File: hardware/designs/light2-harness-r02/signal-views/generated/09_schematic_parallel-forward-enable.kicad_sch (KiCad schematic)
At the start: 45 parts, among them J2 ESP32-P4 Right Header (EXT1), J3 ESP32-P4 Left Header (EXT2), U1 SN74LVC244AN, U2 SN74LVC244AN, U3 SN74LV125AN, U4 SN74LV125AN

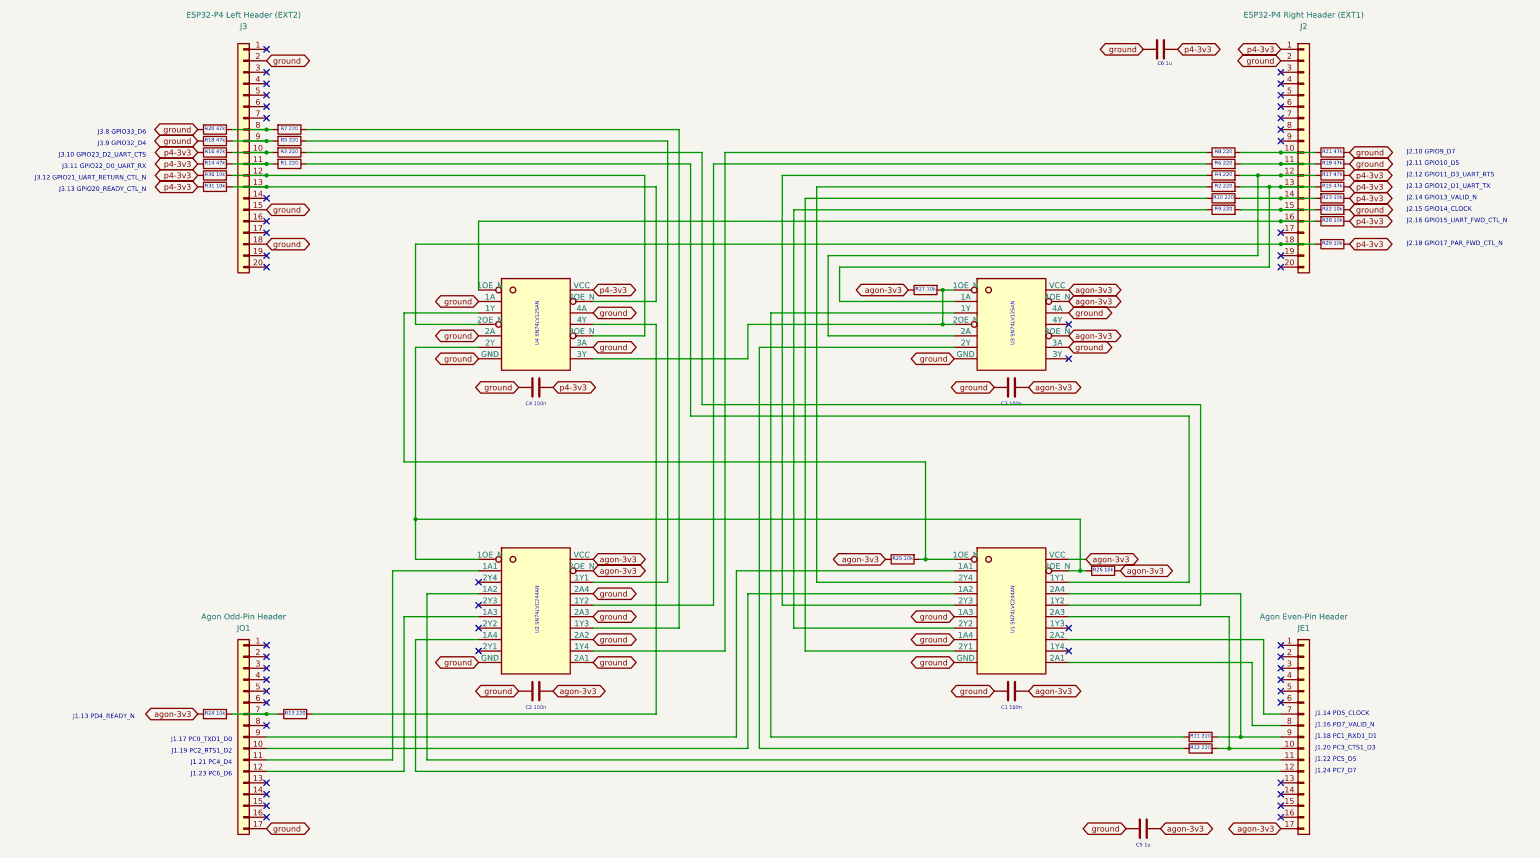
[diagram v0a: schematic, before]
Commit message: HW-001: freeze r02 schematic and ordered signal views
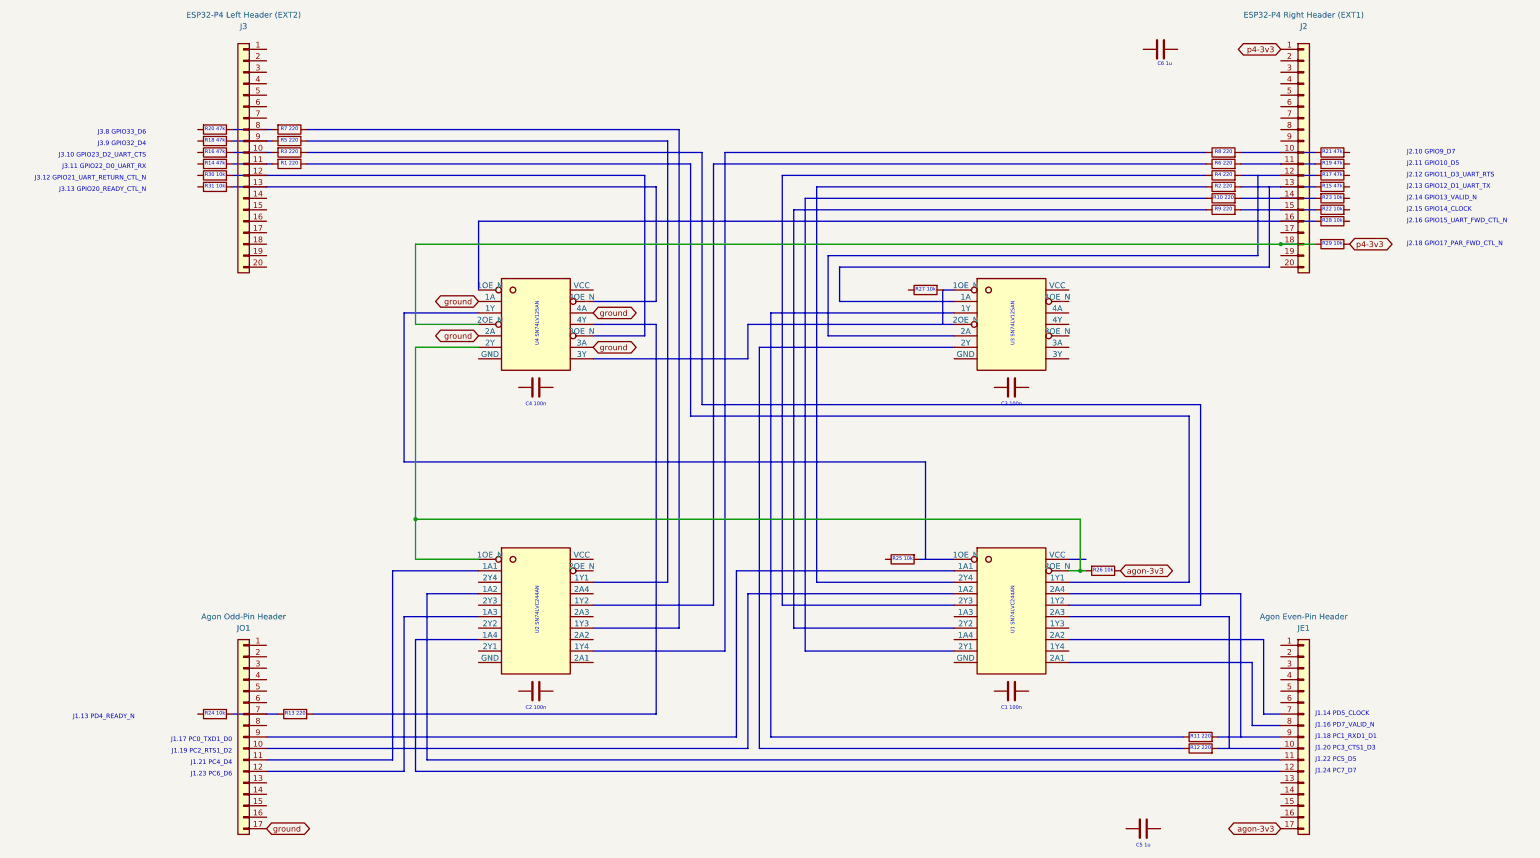
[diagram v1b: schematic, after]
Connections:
- net agon-3v3: no longer C1.2, C2.2, C3.2, C5.2, R24.1, R25.1, R27.1, U1.20 (VCC), U2.19 (2OE_N), U2.20 (VCC), U3.10 (3OE_N), U3.13 (4OE_N), U3.14 (VCC)
- net ground: no longer C1.1, C2.1, C3.1, C4.1, C5.1, C6.2, J2.2 (Pin_2), J3.15 (Pin_15), J3.18 (Pin_18), J3.2 (Pin_2), R18.2, R19.2, R20.2, R21.2, R22.2, U1.10 (GND), U1.6 (1A3), U1.8 (1A4), U2.10 (GND), U2.11 (2A1), U2.13 (2A2), U2.15 (2A3), U2.17 (2A4), U3.12 (4A), U3.7 (GND), U3.9 (3A), U4.7 (GND)
- net p4-3v3: no longer C4.2, C6.1, R14.1, R15.1, R16.1, R17.1, R23.1, R28.1, R30.1, R31.1, U4.14 (VCC)
- net at R11.1: no longer U3.3 (1Y)
- net at R5.1: no longer U2.18 (1Y1)
- net at R13.2: no longer U4.11 (4Y)
- net at R6.1: no longer U2.16 (1Y2)
- net at R7.1: no longer U2.14 (1Y3)
- net at U2.12 (1Y4): no longer R8.1
- net at U2.2 (1A1): no longer JO1.11 (Pin_11)
- net at U2.4 (1A2): no longer JE1.11 (Pin_11)
- net at U2.6 (1A3): no longer JO1.12 (Pin_12)
- net at U2.8 (1A4): no longer JE1.12 (Pin_12)
- net at R3.1: no longer U1.16 (1Y2)
- net at R1.1: no longer U1.18 (1Y1)
- net at R2.1: no longer U1.3 (2Y4)
- net at R10.1: no longer U1.9 (2Y1)
- net at R12.1: no longer U3.6 (2Y)
- net at R4.1: no longer U1.5 (2Y3)
- net at R9.1: no longer U1.7 (2Y2)
- net at JO1.10 (Pin_10): no longer U1.4 (1A2)
- net at JO1.9 (Pin_9): no longer U1.2 (1A1)
- net at JE1.7 (Pin_7): no longer U1.13 (2A2)
- net at JE1.8 (Pin_8): no longer U1.11 (2A1)
- now unconnected: J2.10 (Pin_10), J2.11 (Pin_11), J2.12 (Pin_12), J2.13 (Pin_13), J2.14 (Pin_14), J2.15 (Pin_15), J2.16 (Pin_16), J3.10 (Pin_10), J3.11 (Pin_11), J3.12 (Pin_12), J3.13 (Pin_13), J3.8 (Pin_8), J3.9 (Pin_9), JE1.10 (Pin_10), JE1.9 (Pin_9), JO1.7 (Pin_7), R1.2, R10.2, R11.2, R12.2, R13.1, R14.2, R15.2, R16.2, R17.2, R18.1, R19.1, R2.2, R20.1, R21.1, R22.1, R23.2, R24.2, R25.2, R27.2, R28.2, R3.2, R30.2, R31.2, R4.2, R5.2, R6.2, R7.2, R8.2, R9.2, U1.1 (1OE_N), U1.15 (2A3), U1.17 (2A4), U3.1 (1OE_N), U3.2 (1A), U3.4 (2OE_N), U3.5 (2A), U4.1 (1OE_N), U4.10 (3OE_N), U4.13 (4OE_N), U4.3 (1Y), U4.8 (3Y)
- no-connect marks 50 -> 0
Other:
- title: Light 2 harness r02 — PHYSICAL TOP-VIEW DIP DIRECT-WIRE AID -> Light 2 harness r02 — Parallel forward enable — FUNCTION VIEW, NOT AUTHORITY
